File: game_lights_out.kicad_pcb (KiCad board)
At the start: 2 copper layers, 171.2 x 136.9 mm, 94 parts, among them SW1 SW_MEC_5E, SW10 SW_MEC_5E, SW11 SW_MEC_5E, SW12 SW_MEC_5E, SW13 SW_MEC_5E, SW14 SW_MEC_5E, SW15 SW_MEC_5E, SW16 SW_MEC_5E, SW17 SW_MEC_5E, SW18 SW_MEC_5E, SW19 SW_MEC_5E, SW2 SW_MEC_5E, SW20 SW_MEC_5E, SW21 SW_MEC_5E, SW22 SW_MEC_5E, SW23 SW_MEC_5E, SW24 SW_MEC_5E, SW25 SW_MEC_5E, SW26 SW_MEC_5E, SW27 SW_MEC_5E, SW28 SW_MEC_5E, SW29 SW_MEC_5E, SW3 SW_MEC_5E, SW30 SW_MEC_5E, SW31 SW_MEC_5E, SW32 SW_MEC_5E, SW33 SW_MEC_5E, SW34 SW_MEC_5E, SW35 SW_MEC_5E, SW36 SW_MEC_5E, SW37 SW_MEC_5E, SW38 SW_MEC_5E, SW39 SW_MEC_5E, SW4 SW_MEC_5E, SW40 SW_MEC_5E, SW5 SW_MEC_5E, SW6 SW_MEC_5E, SW7 SW_MEC_5E, SW8 SW_MEC_5E, SW9 SW_MEC_5E, U1 ATmega328-P, U2 ULN2803A

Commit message: Minor fixes in routing
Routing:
- net R2: track 183.4 -> 176.9 mm
- net R3: track 168.3 -> 166.3 mm
- net R4: track 152.5 -> 150.6 mm
- net SCTL: track 158.4 -> 160.3 mm
- net R1: track 202.5 -> 200.6 mm
- net R5: track 165.1 -> 163.3 mm

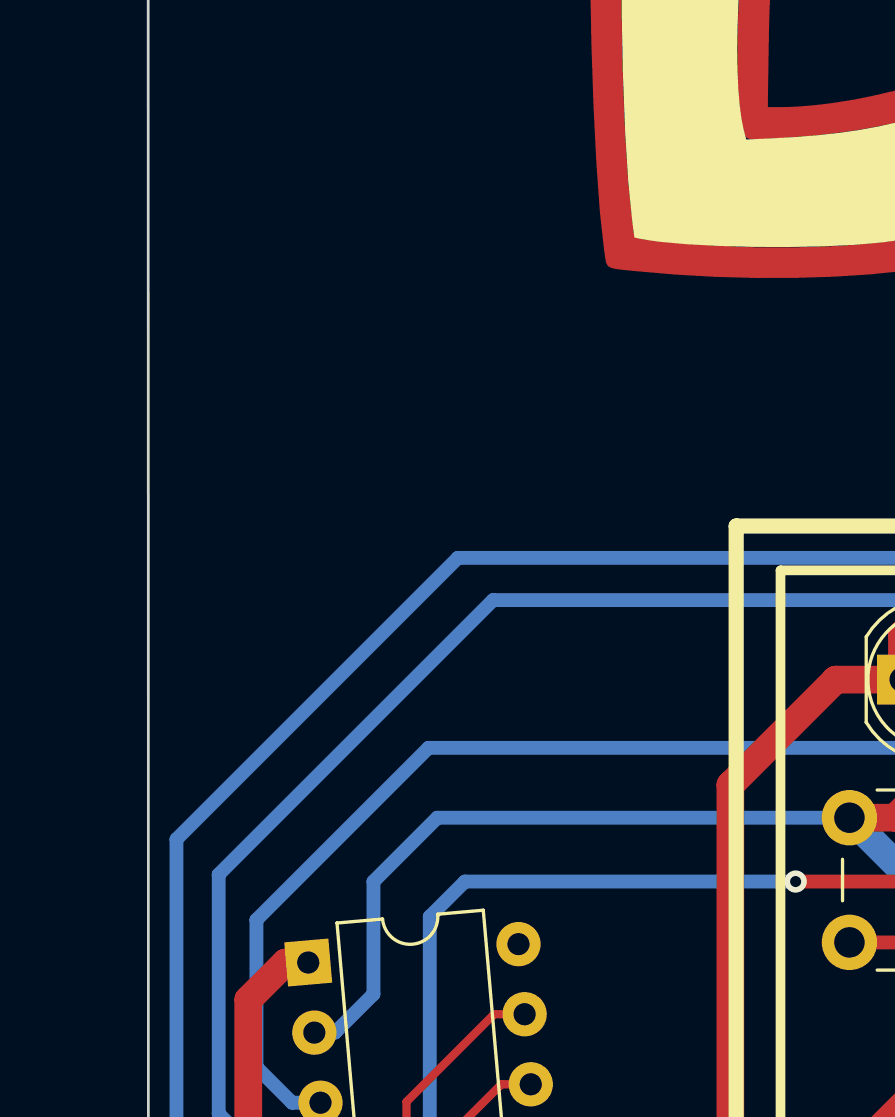
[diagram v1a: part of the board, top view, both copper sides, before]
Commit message: Added speaker
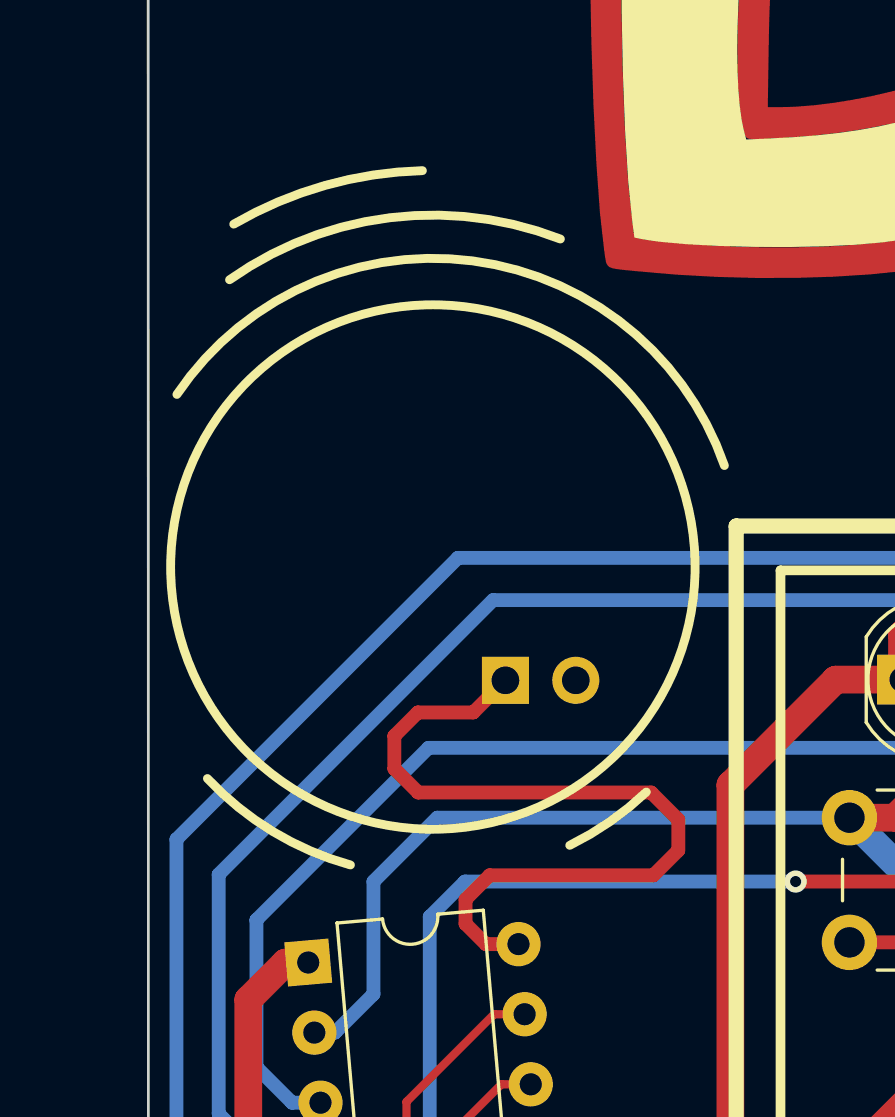
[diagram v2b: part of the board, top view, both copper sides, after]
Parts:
- added LS1: Speaker, Connector_PinHeader_2.54mm:PinHeader_1x02_P2.54mm_Vertical, F.Cu at (40.1, 61.6)
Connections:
- U1 pad 28: unconnected-(U1-PC5-Pad28) -> SPK
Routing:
- net SPK: track 0.00 -> 29.7 mm
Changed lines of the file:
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@@
   (net 72 "Net-(U1-PC3)")
   (net 73 "Net-(U1-PC4)")
-  (net 74 "unconnected-(U1-PC5-Pad28)")
-  (net 75 "unconnected-(U2-I6-Pad6)")
-  (net 76 "unconnected-(U2-I7-Pad7)")
-  (net 77 "unconnected-(U2-I8-Pad8)")
-  (net 78 "unconnected-(U2-O8-Pad11)")
-  (net 79 "unconnected-(U2-O7-Pad12)")
-  (net 80 "unconnected-(U2-O6-Pad13)")
+  (net 74 "unconnected-(U2-I6-Pad6)")
+  (net 75 "unconnected-(U2-I7-Pad7)")
+  (net 76 "unconnected-(U2-I8-Pad8)")
+  (net 77 "unconnected-(U2-O8-Pad11)")
+  (net 78 "unconnected-(U2-O7-Pad12)")
+  (net 79 "unconnected-(U2-O6-Pad13)")
+  (net 80 "SPK")
   (footprint "kicad_footprints:SW_PUSH_6mm_H5mm" (layer "F.Cu")
     (at 68.857145 127.595)
@@
       (net 73 "Net-(U1-PC4)") (pinfunction "I5") (pintype "input"))
     (pad "6" thru_hole oval (at 0 12.7 347) (size 1.6 1.6) (drill 0.8) (layers "*.Cu" "*.Mask")
-      (net 75 "unconnected-(U2-I6-Pad6)") (pinfunction "I6") (pintype "input+no_connect"))
+      (net 74 "unconnected-(U2-I6-Pad6)") (pinfunction "I6") (pintype "input+no_connect"))
     (pad "7" thru_hole oval (at 0 15.24 347) (size 1.6 1.6) (drill 0.8) (layers "*.Cu" "*.Mask")
-      (net 76 "unconnected-(U2-I7-Pad7)") (pinfunction "I7") (pintype "input+no_connect"))
+      (net 75 "unconnected-(U2-I7-Pad7)") (pinfunction "I7") (pintype "input+no_connect"))
     (pad "8" thru_hole oval (at 0 17.78 347) (size 1.6 1.6) (drill 0.8) (layers "*.Cu" "*.Mask")
-      (net 77 "unconnected-(U2-I8-Pad8)") (pinfunction "I8") (pintype "input+no_connect"))
+      (net 76 "unconnected-(U2-I8-Pad8)") (pinfunction "I8") (pintype "input+no_connect"))
     (pad "9" thru_hole oval (at 0 20.32 347) (size 1.6 1.6) (drill 0.8) (layers "*.Cu" "*.Mask")
       (net 1 "GND") (pinfunction "GND") (pintype "power_in"))
@@
       (net 16 "RST") (pinfunction "COM") (pintype "passive"))
     (pad "11" thru_hole oval (at 7.62 17.78 347) (size 1.6 1.6) (drill 0.8) (layers "*.Cu" "*.Mask")
-      (net 78 "unconnected-(U2-O8-Pad11)") (pinfunction "O8") (pintype "open_collector+no_connect"))
+      (net 77 "unconnected-(U2-O8-Pad11)") (pinfunction "O8") (pintype "open_collector+no_connect"))
     (pad "12" thru_hole oval (at 7.62 15.24 347) (size 1.6 1.6) (drill 0.8) (layers "*.Cu" "*.Mask")
-      (net 79 "unconnected-(U2-O7-Pad12)") (pinfunction "O7") (pintype "open_collector+no_connect"))
+      (net 78 "unconnected-(U2-O7-Pad12)") (pinfunction "O7") (pintype "open_collector+no_connect"))
     (pad "13" thru_hole oval (at 7.62 12.7 347) (size 1.6 1.6) (drill 0.8) (layers "*.Cu" "*.Mask")
-      (net 80 "unconnected-(U2-O6-Pad13)") (pinfunction "O6") (pintype "open_collector+no_connect"))
+      (net 79 "unconnected-(U2-O6-Pad13)") (pinfunction "O6") (pintype "open_collector+no_connect"))
     (pad "14" thru_hole oval (at 7.62 10.16 347) (size 1.6 1.6) (drill 0.8) (layers "*.Cu" "*.Mask")
       (net 14 "R5") (pinfunction "O5") (pintype "open_collector"))
@@
       (net 73 "Net-(U1-PC4)") (pinfunction "PC4") (pintype "bidirectional"))
     (pad "28" thru_hole oval (at 7.62 0 5) (size 1.6 1.6) (drill 0.8) (layers "*.Cu" "*.Mask")
-      (net 74 "unconnected-(U1-PC5-Pad28)") (pinfunction "PC5") (pintype "bidirectional+no_connect"))
+      (net 80 "SPK") (pinfunction "PC5") (pintype "bidirectional"))
     (model "${KICAD6_3DMODEL_DIR}/Package_DIP.3dshapes/DIP-28_W7.62mm.wrl"
       (offset (xyz 0 0 0))
@@
     )
   )
+  (footprint "Connector_PinHeader_2.54mm:PinHeader_1x02_P2.54mm_Vertical" (layer "F.Cu")
+    (at 40.07 61.57 90)
+    (descr "Through hole straight pin header, 1x02, 2.54mm pitch, single row")
+    (tags "Through hole pin header THT 1x02 2.54mm single row")
+    (property "Sheetfile" "game_lights_out.kicad_sch")
+    (property "Sheetname" "")
+    (property "ki_description" "Speaker")
+    (property "ki_keywords" "speaker sound")
+    (attr through_hole)
+    (fp_text reference "LS1" (at 0 -2.33 90) (layer "F.SilkS") hide
+        (effects (font (size 1 1) (thickness 0.15)))
+    )
+    (fp_text value "Speaker" (at 0 4.87 90) (layer "F.Fab") hide
+        (effects (font (size 1 1) (thickness 0.15)))
+    )
+    (fp_line (start -1.8 -1.8) (end -1.8 4.35)
+      (stroke (width 0.05) (type solid)) (layer "F.CrtYd"))
+    (fp_line (start -1.8 4.35) (end 1.8 4.35)
+      (stroke (width 0.05) (type solid)) (layer "F.CrtYd"))
+    (fp_line (start 1.8 -1.8) (end -1.8 -1.8)
+      (stroke (width 0.05) (type solid)) (layer "F.CrtYd"))
+    (fp_line (start 1.8 4.35) (end 1.8 -1.8)
+      (stroke (width 0.05) (type solid)) (layer "F.CrtYd"))
+    (pad "1" thru_hole rect (at 0 0 90) (size 1.7 1.7) (drill 1) (layers "*.Cu" "*.Mask")
+      (net 80 "SPK") (pinfunction "1") (pintype "input"))
+    (pad "2" thru_hole oval (at 0 2.54 90) (size 1.7 1.7) (drill 1) (layers "*.Cu" "*.Mask")
+      (net 1 "GND") (pinfunction "2") (pintype "input"))
+    (model "${KICAD6_3DMODEL_DIR}/Connector_PinHeader_2.54mm.3dshapes/PinHeader_1x02_P2.54mm_Vertical.wrl" hide
+      (offset (xyz 0 0 0))
+      (scale (xyz 1 1 1))
+      (rotate (xyz 0 0 0))
+    )
+  )
   (footprint "LED_THT:LED_D5.0mm" (layer "F.Cu")
     (at 54.395 142.955)
@@
   (gr_arc (start 193.120201 119.802441) (mid 194.497915 123.40978) (end 191.382143 125.690778)
     (stroke (width 0.48) (type solid)) (layer "F.SilkS"))
+  (gr_arc (start 45.15594 65.60299) (mid 43.846626 66.66954) (end 42.3918 67.527044)
+    (stroke (width 0.32) (type default)) (layer "F.SilkS"))
   (gr_poly
     (pts
@@
   (gr_line (start 50 154.8) (end 50 57.6)
     (stroke (width 0.35) (type default)) (layer "F.SilkS"))
+  (gr_arc (start 28.21 51.25) (mid 38.885322 46.42874) (end 47.974884 53.817035)
+    (stroke (width 0.32) (type default)) (layer "F.SilkS"))
+  (gr_arc (start 30.110001 47.110001) (mid 35.896935 44.870462) (end 42.054345 45.638865)
+    (stroke (width 0.32) (type default)) (layer "F.SilkS"))
+  (gr_circle (center 37.45 57.48) (end 46.78 55.88)
+    (stroke (width 0.32) (type default)) (fill none) (layer "F.SilkS"))
   (gr_line (start 48.4 156.4) (end 48.4 56)
     (stroke (width 0.55) (type default)) (layer "F.SilkS"))
@@
   (gr_line (start 177.6 156.4) (end 177.6 56)
     (stroke (width 0.55) (type default)) (layer "F.SilkS"))
+  (gr_arc (start 34.47543 68.23567) (mid 31.678139 67.030818) (end 29.310798 65.114519)
+    (stroke (width 0.32) (type default)) (layer "F.SilkS"))
   (gr_poly
     (pts
@@
     )
     (stroke (width 0) (type solid)) (fill solid) (layer "F.SilkS"))
+  (gr_arc (start 30.260632 45.102037) (mid 33.545592 43.708414) (end 37.073183 43.170598)
+    (stroke (width 0.32) (type default)) (layer "F.SilkS"))
   (gr_line (start 189.182143 146.106742) (end 189.182143 146.111742)
     (stroke (width 1.5) (type solid)) (layer "F.SilkS"))
@@
   (segment (start 33.21493 124.63493) (end 34.055144 124.63493) (width 0.3) (layer "F.Cu") (net 73))
   (segment (start 31.496 122.916) (end 33.21493 124.63493) (width 0.3) (layer "F.Cu") (net 73))
+  (segment (start 36.92 65.62) (end 45.33 65.62) (width 0.5) (layer "F.Cu") (net 80))
+  (segment (start 40.07 61.57) (end 38.91 62.73) (width 0.5) (layer "F.Cu") (net 80))
+  (segment (start 36.06 64.76) (end 36.92 65.62) (width 0.5) (layer "F.Cu") (net 80))
+  (segment (start 38.63 69.48) (end 38.63 70.36) (width 0.5) (layer "F.Cu") (net 80))
+  (segment (start 39.363531 71.093531) (end 40.541375 71.093531) (width 0.5) (layer "F.Cu") (net 80))
+  (segment (start 46.31 66.6) (end 46.31 67.71) (width 0.5) (layer "F.Cu") (net 80))
+  (segment (start 36.06 63.58) (end 36.06 64.76) (width 0.5) (layer "F.Cu") (net 80))
+  (segment (start 45.41 68.61) (end 39.5 68.61) (width 0.5) (layer "F.Cu") (net 80))
+  (segment (start 45.33 65.62) (end 46.31 66.6) (width 0.5) (layer "F.Cu") (net 80))
+  (segment (start 38.63 70.36) (end 39.363531 71.093531) (width 0.5) (layer "F.Cu") (net 80))
+  (segment (start 38.91 62.73) (end 36.91 62.73) (width 0.5) (layer "F.Cu") (net 80))
+  (segment (start 46.31 67.71) (end 45.41 68.61) (width 0.5) (layer "F.Cu") (net 80))
+  (segment (start 36.91 62.73) (end 36.06 63.58) (width 0.5) (layer "F.Cu") (net 80))
+  (segment (start 39.5 68.61) (end 38.63 69.48) (width 0.5) (layer "F.Cu") (net 80))
   (zone (net 1) (net_name "GND") (layer "B.Cu") (name "GROUND") (hatch edge 0.508)
     (connect_pads (clearance 0.32))

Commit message: Minor fixes on decorations
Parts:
- moved LS1 3.38 mm to (43.4, 60.9), turned to 157 degrees
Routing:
- net C4: track 207.7 -> 212.4 mm
- net C3: track 185.0 -> 189.5 mm
- net SPK: track 29.7 -> 33.2 mm
- net C6: track 266.9 -> 266.2 mm

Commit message: Board clean up - Remove mounting holes - Remove component outlines - Remove matrix outline - Add SMD pads for power
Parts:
- removed H1, H2, H3, H4: MountingHole_Pad, MountingHole:MountingHole_2.5mm_Pad
- added REF**: SolderWirePad_1x01_SMD_5x10mm, Connector_Wire:SolderWirePad_1x01_SMD_5x10mm, B.Cu at (48.3, 76.3)
- added REF**: SolderWirePad_1x01_SMD_5x10mm, Connector_Wire:SolderWirePad_1x01_SMD_5x10mm, B.Cu at (48.3, 82.5)
- moved SW_CTL1 2.45 mm to (185.0, 120.9)
- moved LS1 1.84 mm to (42.3, 62.4), turned to 142 degrees
- moved R2 1.60 mm to (185.5, 102.5)
- moved R3 0.72 mm to (191.9, 103.0)
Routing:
- net RST: track 225.0 -> 108.8 mm, vias 2 -> 0
- net C2: track 158.1 -> 165.4 mm
- net Net-(DMOD1-A): track 4.88 -> 6.52 mm
- net SPK: track 33.2 -> 31.6 mm
- net Net-(DMOD2-A): track 5.59 -> 6.36 mm
- net LD1: track 286.2 -> 287.0 mm
- net LD2: track 268.7 -> 268.1 mm
- net SCTL: track 160.3 -> 160.9 mm

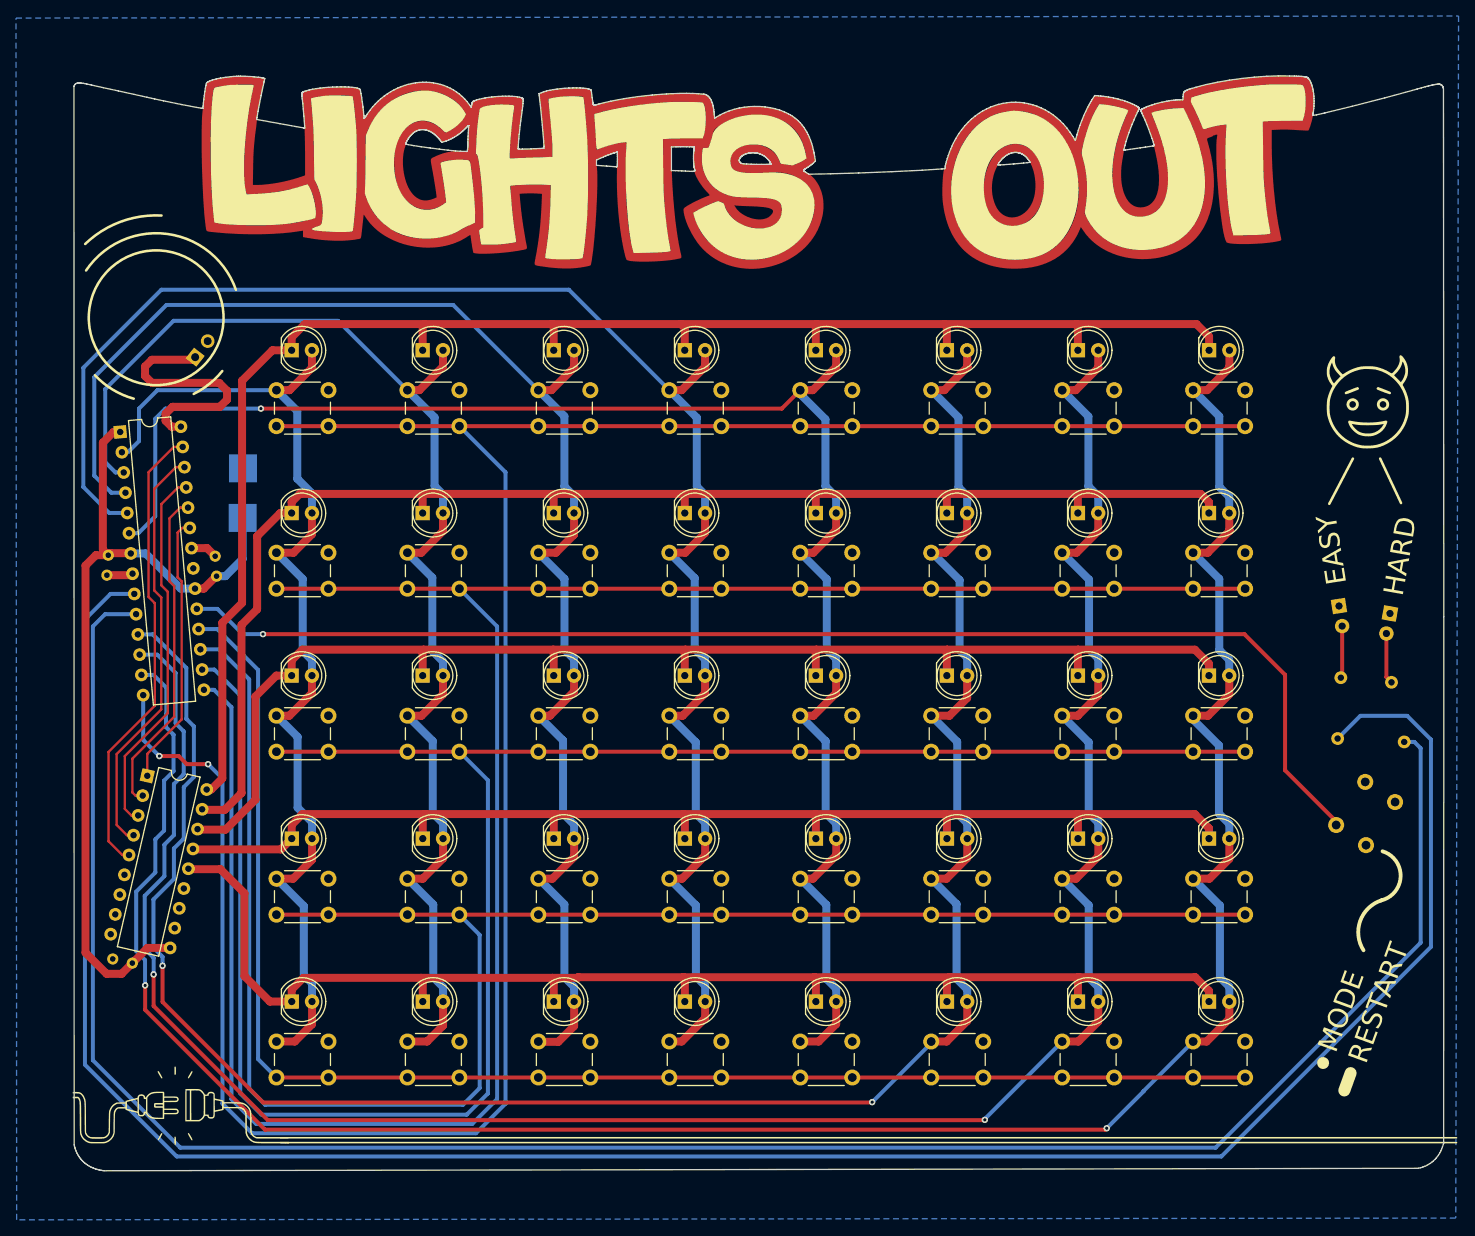
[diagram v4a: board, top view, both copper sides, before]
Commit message: Added mounting holes
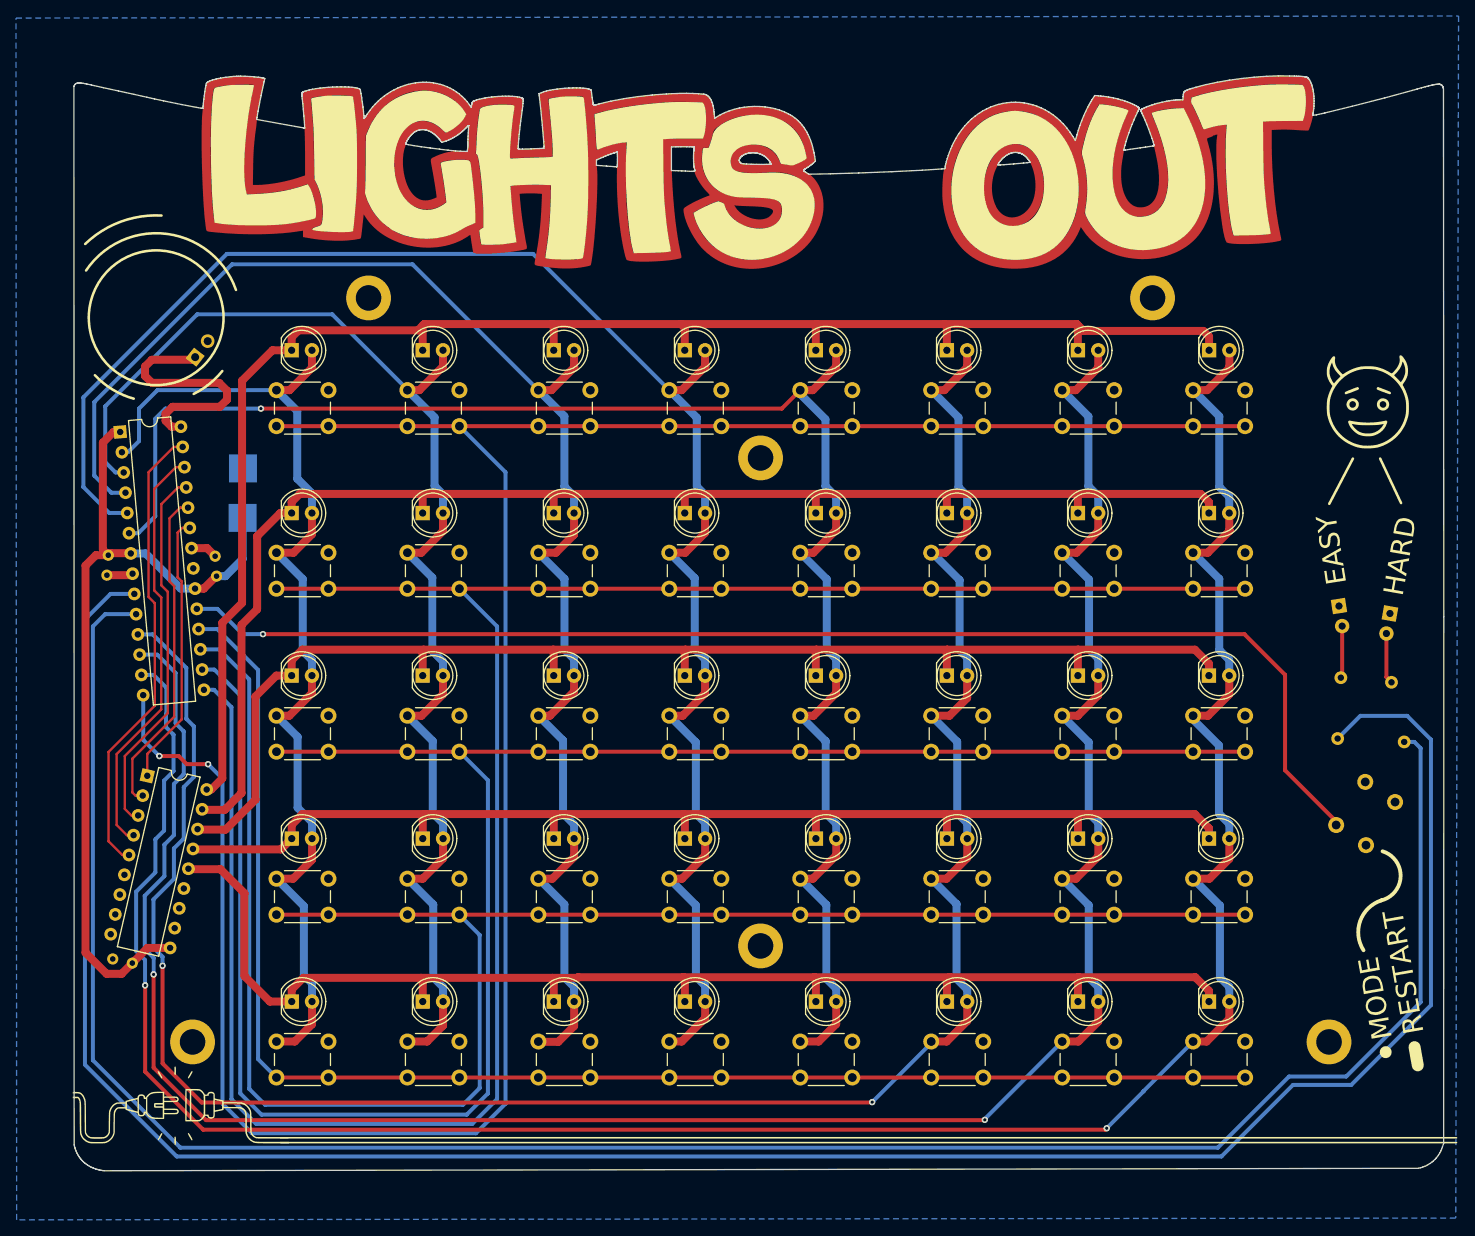
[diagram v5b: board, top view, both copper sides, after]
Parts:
- added REF**: MountingHole_3.2mm_M3_DIN965_Pad, MountingHole:MountingHole_3.2mm_M3_DIN965_Pad, F.Cu at (42.0, 148.0)
- added REF**: MountingHole_3.2mm_M3_DIN965_Pad, MountingHole:MountingHole_3.2mm_M3_DIN965_Pad, F.Cu at (64.0, 55.0)
- added REF**: MountingHole_3.2mm_M3_DIN965_Pad, MountingHole:MountingHole_3.2mm_M3_DIN965_Pad, F.Cu at (113.0, 136.0)
- added REF**: MountingHole_3.2mm_M3_DIN965_Pad, MountingHole:MountingHole_3.2mm_M3_DIN965_Pad, F.Cu at (113.0, 75.0)
- added REF**: MountingHole_3.2mm_M3_DIN965_Pad, MountingHole:MountingHole_3.2mm_M3_DIN965_Pad, F.Cu at (184.1, 148.0)
- added REF**: MountingHole_3.2mm_M3_DIN965_Pad, MountingHole:MountingHole_3.2mm_M3_DIN965_Pad, F.Cu at (162.0, 55.0)
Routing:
- net C8: track 297.4 -> 301.9 mm
- net C7: track 282.2 -> 286.7 mm
- net C6: track 266.2 -> 270.8 mm
- net LD2: track 268.1 -> 272.4 mm
- net LD1: track 287.0 -> 291.3 mm
- net C3: track 189.5 -> 191.9 mm
- net C4: track 212.3 -> 213.8 mm
- net C2: track 165.4 -> 164.8 mm
